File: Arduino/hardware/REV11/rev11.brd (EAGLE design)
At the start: 79 x 79 mm, 31 parts, among them IC2 ATMEGA168-AU, Q1 32768Hz

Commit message: updates to both rev10 and rev11
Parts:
- moved ANT 81.5 mm to (1.27, 34.9), turned to 0 degrees
- moved R1 79.0 mm to (74.9, 50.8)
- moved R3 79.0 mm to (74.9, 47.0)
- moved PHT1 73.3 mm to (76.2, 36.8)
- moved U$4 61.0 mm to (65.0, 2.73)
- moved JP1 52.3 mm to (30.5, 16.5), turned to 270 degrees
- moved U$1 49.8 mm to (76.9, 21.1)
- moved LED 45.4 mm to (47.4, 49.4), turned to 270 degrees
- moved R9 42.8 mm to (59.7, 21.6)
- moved U$2 41.7 mm to (82.4, 4.86)
- moved Q1 40.5 mm to (46.1, 27.9), turned to 270 degrees
- moved + 37.1 mm to (20.0, 43.5), turned to 0 degrees
- moved R7 36.6 mm to (47.7, 41.6), turned to 90 degrees
- moved RFM23B 33.3 mm to (58.8, 41.2), turned to 270 degrees
- moved C9 31.0 mm to (39.5, 27.4)
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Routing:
- net N$31: track 86.7 -> 85.1 mm
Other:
- board size 79 x 79 mm -> 72 x 53 mm
- board text added: "*"
- board text removed: "GND"

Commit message: updates to rev11
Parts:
- removed R3: (no value), resistor:0309V
- moved LED 26.5 mm to (69.7, 35.2), turned to 180 degrees
- moved PHT1 14.6 mm to (67.9, 48.9)
- moved R1 8.98 mm to (68.6, 44.5)
- moved ANT 2.00 mm to (1.27, 32.9)
- moved RFM23B 2.00 mm to (56.8, 41.2)
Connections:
- net GND: no longer R3.1
- net LDR: no longer R3.2

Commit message: updates to rev11
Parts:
- moved R7 21.5 mm to (67.0, 32.4), turned to 0 degrees
- moved R1 16.9 mm to (52.1, 48.3)
- moved PHT1 8.94 mm to (59.0, 48.9)
- moved Q1 4.58 mm to (42.3, 25.3)
- moved C7 4.02 mm to (51.4, 24.9)
- moved C4 4.02 mm to (54.9, 24.9)
- moved C8 4.02 mm to (59.0, 24.9)
- moved RFM23B 3.82 mm to (56.5, 37.4)
- moved C11 3.81 mm to (59.9, 15.1)
- moved R10 3.81 mm to (59.9, 10.9)
- moved R5 3.81 mm to (59.9, 3.91)
- moved R4 3.81 mm to (59.9, 7.72)
- moved R9 3.81 mm to (59.7, 17.8)
- moved C9 2.84 mm to (37.0, 28.6)
- moved LED 2.79 mm to (67.1, 36.0), turned to 270 degrees
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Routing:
- net N$31: track 85.1 -> 86.0 mm
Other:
- board size 72 x 53 mm -> 71 x 53 mm

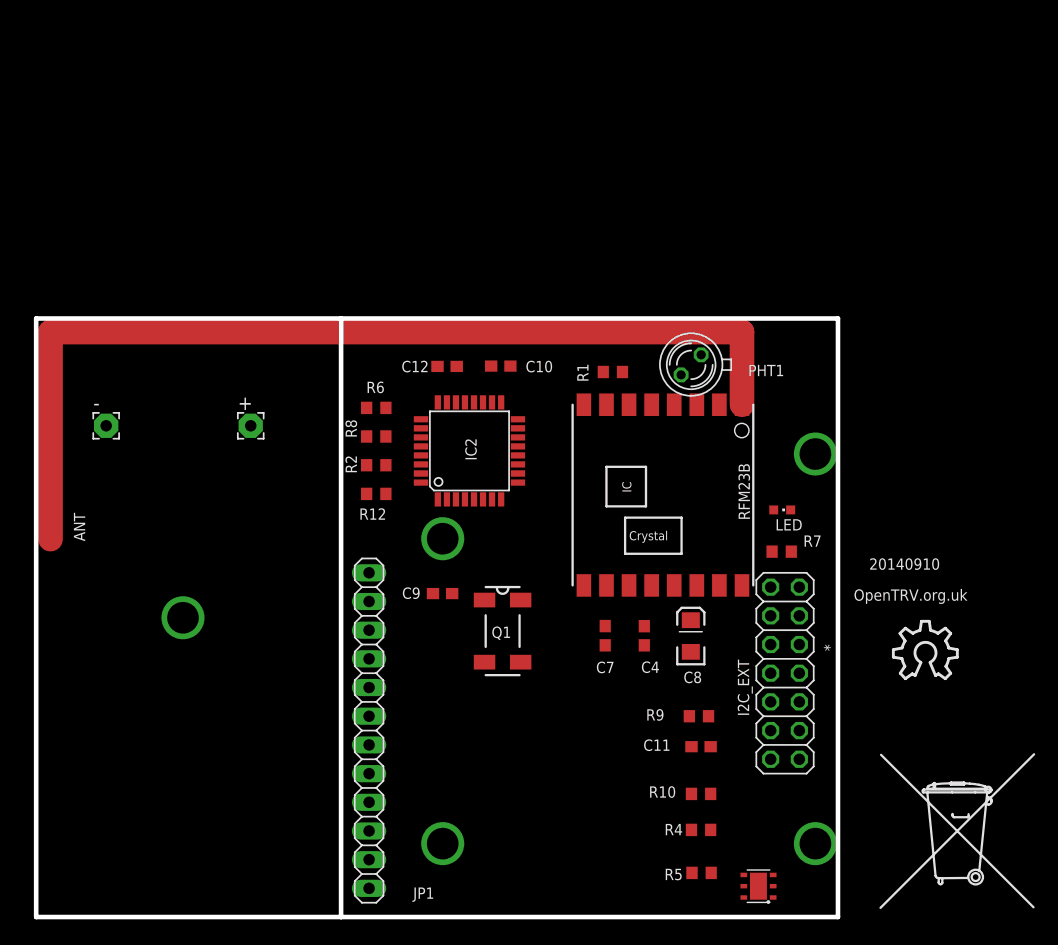
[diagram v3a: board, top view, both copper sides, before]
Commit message: updates to rev 10 & 11
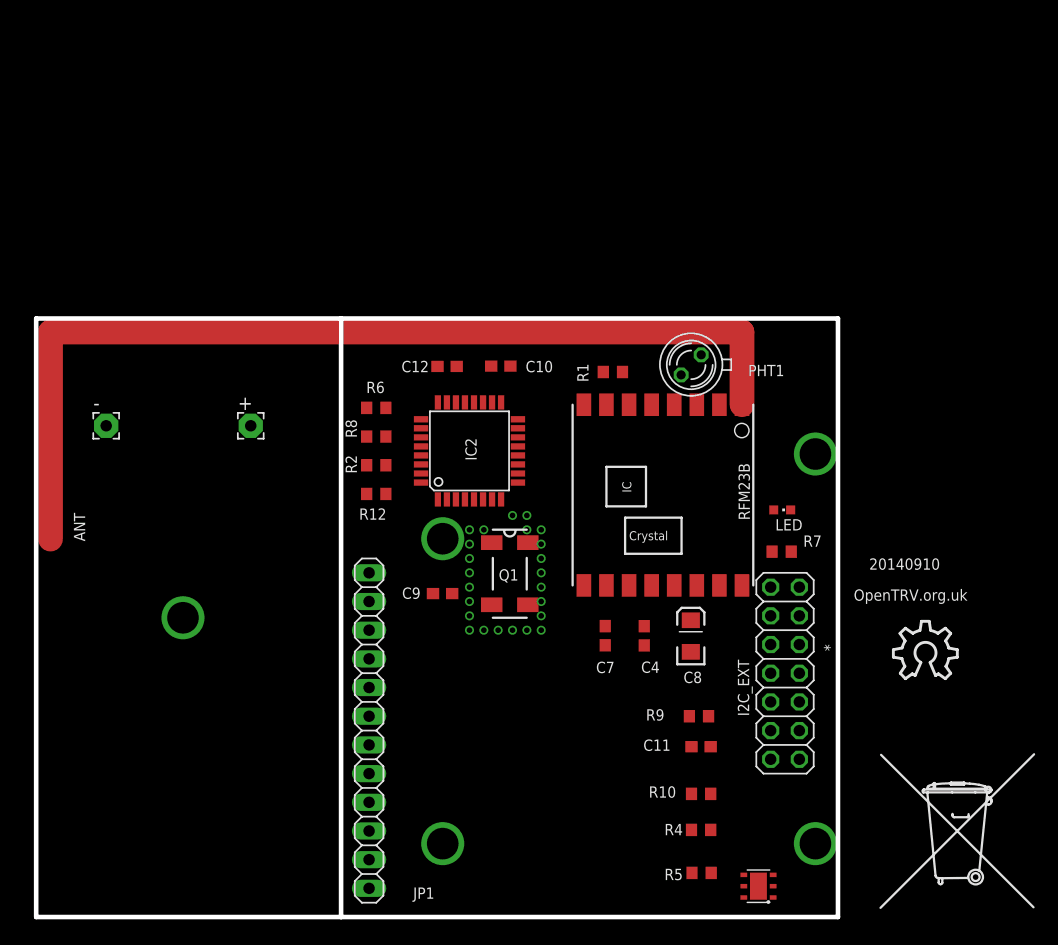
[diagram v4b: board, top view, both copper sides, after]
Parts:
- moved Q1 5.12 mm to (42.9, 30.4)
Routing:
- added copper zone on layer 16, net GND
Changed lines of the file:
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@@
 <attribute name="NAME" x="28.4" y="40.90808125" size="1" layer="25" font="vector" rot="R270"/>
 </element>
-<element name="Q1" library="crystal" package="MC-306" value="32768Hz" x="42.303484375" y="25.3201125" smashed="yes" rot="R270">
-<attribute name="OC_NEWARK" value="31M5576" x="42.303484375" y="25.3201125" size="1.778" layer="27" rot="R270" display="off"/>
-<attribute name="MPN" value="MC-306 60.0KHZ  100PPM ,12.5PF" x="42.303484375" y="25.3201125" size="1.778" layer="27" rot="R270" display="off"/>
-<attribute name="MF" value="" x="42.303484375" y="25.3201125" size="1.778" layer="27" rot="R270" display="off"/>
-<attribute name="OC_FARNELL" value="1278040" x="42.303484375" y="25.3201125" size="1.778" layer="27" rot="R270" display="off"/>
-<attribute name="NAME" x="43.0779125" y="25.711959375" size="1" layer="25" font="vector" rot="R180"/>
+<element name="Q1" library="crystal" package="MC-306" value="32768Hz" x="42.938484375" y="30.4001125" smashed="yes" rot="R270">
+<attribute name="OC_NEWARK" value="31M5576" x="42.938484375" y="30.4001125" size="1.778" layer="27" rot="R270" display="off"/>
+<attribute name="MPN" value="MC-306 60.0KHZ  100PPM ,12.5PF" x="42.938484375" y="30.4001125" size="1.778" layer="27" rot="R270" display="off"/>
+<attribute name="MF" value="" x="42.938484375" y="30.4001125" size="1.778" layer="27" rot="R270" display="off"/>
+<attribute name="OC_FARNELL" value="1278040" x="42.938484375" y="30.4001125" size="1.778" layer="27" rot="R270" display="off"/>
+<attribute name="NAME" x="43.7129125" y="30.791959375" size="1" layer="25" font="vector" rot="R180"/>
 </element>
 <element name="C9" library="resistor" package="C0603" value="100nF" x="36.988065625" y="28.641453125" smashed="yes">
@@
 <wire x1="30.48" y1="2.54" x2="37.838065625" y2="28.641453125" width="0" layer="19" extent="1-1"/>
 <wire x1="7.2" y1="43.5" x2="36.5393875" y2="48.75630625" width="0" layer="19" extent="1-1"/>
+<polygon width="0.4064" layer="16">
+<vertex x="1" y="53"/>
+<vertex x="1" y="0"/>
+<vertex x="72" y="0"/>
+<vertex x="72" y="53"/>
+</polygon>
 </signal>
 <signal name="D6">
@@
 <contactref element="Q1" pad="4"/>
 <contactref element="IC2" pad="8"/>
-<wire x1="42.17" y1="36.9824" x2="43.903484375" y2="28.0701125" width="0" layer="19" extent="1-1"/>
+<wire x1="42.17" y1="36.9824" x2="44.538484375" y2="33.1501125" width="0" layer="19" extent="1-1"/>
 </signal>
 <signal name="XTAL2">
 <contactref element="Q1" pad="1"/>
 <contactref element="IC2" pad="7"/>
-<wire x1="40.703484375" y1="28.0701125" x2="41.37" y2="36.9824" width="0" layer="19" extent="1-1"/>
+<wire x1="41.338484375" y1="33.1501125" x2="41.37" y2="36.9824" width="0" layer="19" extent="1-1"/>
 </signal>
 <signal name="TX">
@@
 <via x="70" y="6.5" extent="1-16" drill="2.8"/>
 </signal>
+<signal name="N$11">
+<via x="40.64" y="25.4" extent="1-16" drill="0.5"/>
+</signal>
+<signal name="N$12">
+<via x="41.91" y="25.4" extent="1-16" drill="0.5"/>
+</signal>
+<signal name="N$14">
+<via x="43.18" y="25.4" extent="1-16" drill="0.5"/>
+</signal>
+<signal name="N$15">
+<via x="44.45" y="25.4" extent="1-16" drill="0.5"/>
+</signal>
+<signal name="N$16">
+<via x="45.72" y="25.4" extent="1-16" drill="0.5"/>
+</signal>
+<signal name="N$17">
+<via x="45.72" y="26.67" extent="1-16" drill="0.5"/>
+</signal>
+<signal name="N$19">
+<via x="45.72" y="27.94" extent="1-16" drill="0.5"/>
+</signal>
+<signal name="N$20">
+<via x="45.72" y="29.21" extent="1-16" drill="0.5"/>
+</signal>
+<signal name="N$21">
+<via x="45.72" y="30.48" extent="1-16" drill="0.5"/>
+</signal>
+<signal name="N$22">
+<via x="45.72" y="31.75" extent="1-16" drill="0.5"/>
+</signal>
+<signal name="N$24">
+<via x="45.72" y="33.02" extent="1-16" drill="0.5"/>
+</signal>
+<signal name="N$25">
+<via x="45.72" y="34.29" extent="1-16" drill="0.5"/>
+</signal>
+<signal name="N$26">
+<via x="44.45" y="34.29" extent="1-16" drill="0.5"/>
+</signal>
+<signal name="N$28">
+<via x="44.45" y="35.56" extent="1-16" drill="0.5"/>
+</signal>
+<signal name="N$30">
+<via x="43.18" y="35.56" extent="1-16" drill="0.5"/>
+</signal>
+<signal name="N$32">
+<via x="39.37" y="33.02" extent="1-16" drill="0.5"/>
+</signal>
+<signal name="N$33">
+<via x="39.37" y="31.75" extent="1-16" drill="0.5"/>
+</signal>
+<signal name="N$34">
+<via x="39.37" y="30.48" extent="1-16" drill="0.5"/>
+</signal>
+<signal name="N$35">
+<via x="39.37" y="29.21" extent="1-16" drill="0.5"/>
+</signal>
+<signal name="N$36">
+<via x="39.37" y="27.94" extent="1-16" drill="0.5"/>
+</signal>
+<signal name="N$37">
+<via x="39.37" y="26.67" extent="1-16" drill="0.5"/>
+</signal>
+<signal name="N$38">
+<via x="39.37" y="25.4" extent="1-16" drill="0.5"/>
+</signal>
+<signal name="N$39">
+<via x="40.64" y="34.29" extent="1-16" drill="0.5"/>
+</signal>
+<signal name="N$40">
+<via x="39.37" y="34.29" extent="1-16" drill="0.5"/>
+</signal>
 </signals>

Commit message: bringing things back in sync
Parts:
- renumbered R1 to R1********
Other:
- board text added: "20151110"
- board text removed: "20140910"
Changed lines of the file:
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@@
 <board>
 <plain>
-<text x="81.041028125" y="31.75376875" size="1" layer="25" font="vector" rot="R180">20140910</text>
-<text x="73.245621875" y="1.250803125" size="1" layer="22" font="vector" rot="MR90">License: http://goo.gl/3d71UJ</text>
-<text x="73.391121875" y="28.01046875" size="1" layer="25" font="vector">OpenTRV.org.uk</text>
+<text x="48.021028125" y="16.51376875" size="1" layer="25" font="vector" rot="R180">20151110</text>
+<text x="26.689196875" y="0.855621875" size="1" layer="22" font="vector" rot="MR0">License: http://goo.gl/3d71UJ</text>
+<text x="41.641121875" y="2.61046875" size="1" layer="25" font="vector">OpenTRV.org.uk</text>
 <text x="70.353415625" y="24.155434375" size="1" layer="25" font="vector" rot="SR270">*</text>
 <wire x1="1" y1="53" x2="1" y2="0" width="0.4064" layer="20"/>
@@
 <attribute name="NAME" x="4.34" y="35.79" size="1" layer="25" rot="R270"/>
 </element>
-<element name="R1" library="resistor" package="R0603" value="220K" x="52.07" y="48.26" smashed="yes">
+<element name="R1********" library="resistor" package="R0603" value="220K" x="52.07" y="48.26" smashed="yes">
 <attribute name="NAME" x="49.911" y="47.371" size="1" layer="25" rot="R90"/>
 </element>
@@
 <contactref element="U$4" pad="2"/>
 <contactref element="I2C_EXT" pad="6"/>
-<contactref element="R1" pad="2"/>
+<contactref element="R1********" pad="2"/>
 <contactref element="JP1" pad="12"/>
 <contactref element="-" pad="1"/>
@@
 </signal>
 <signal name="LDR">
-<contactref element="R1" pad="1"/>
+<contactref element="R1********" pad="1"/>
 <contactref element="IC2" pad="23"/>
 <contactref element="PHT1" pad="K"/>

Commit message: Bo's update.
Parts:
- R1: value 220K -> 100K
- moved Q1 0.48 mm to (42.5, 30.2)
- renumbered R1******** to R1
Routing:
- net GND: track 0.00 -> 204.1 mm
- net VCC: track 0.00 -> 203.9 mm, vias 0 -> 7
- net SDA: track 0.00 -> 90.3 mm, vias 0 -> 4
- net D7: track 0.00 -> 89.6 mm, vias 0 -> 1
- net SCL: track 0.00 -> 80.7 mm, vias 0 -> 2
- net D2: track 0.00 -> 73.2 mm, vias 0 -> 3
- net SPI_NSS: track 0.00 -> 57.9 mm, vias 0 -> 4
- net TX: track 0.00 -> 52.8 mm, vias 0 -> 2
- net A7: track 0.00 -> 49.6 mm, vias 0 -> 1
- net RESET: track 0.00 -> 48.2 mm, vias 0 -> 4
- net RX: track 0.00 -> 47.9 mm, vias 0 -> 2
- net RFM_IRQ: track 0.00 -> 47.0 mm, vias 0 -> 2
- net SPI_MISO: track 0.00 -> 45.3 mm, vias 0 -> 2
- net SPI_MOSI: track 0.00 -> 44.7 mm, vias 0 -> 2
- net D6: track 0.00 -> 42.4 mm, vias 0 -> 3
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- added copper zone on layer 1, net GND
- removed copper zone on layer 16, net GND

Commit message: rev11 touch up
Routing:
- net A3: track 22.4 -> 62.0 mm, vias 1 -> 4
- net A7: track 49.6 -> 85.5 mm, vias 1 -> 3
- net SPI_NSS: track 57.9 -> 90.8 mm, vias 4 -> 6
- net LED_HEATCALL_L: track 33.0 -> 56.7 mm, vias 2 -> 4
- net SCL: track 80.7 -> 102.9 mm
- net GND: track 204.1 -> 224.6 mm
- net D7: track 89.6 -> 74.7 mm, vias 1 -> 3
- net SDA: track 90.3 -> 101.4 mm
- net RFM_IRQ: track 47.0 -> 57.4 mm
- net N$6: track 15.5 -> 5.27 mm, vias 4 -> 2
- net SPI_MISO: track 45.3 -> 35.4 mm, vias 2 -> 4
- net RX: track 47.9 -> 56.9 mm
- net N$4: track 19.7 -> 11.0 mm, vias 0 -> 1
- net A6: track 34.5 -> 42.0 mm, vias 1 -> 3
- net VCC: track 203.9 -> 210.4 mm, vias 7 -> 9
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- removed copper zone on layer 1, net GND

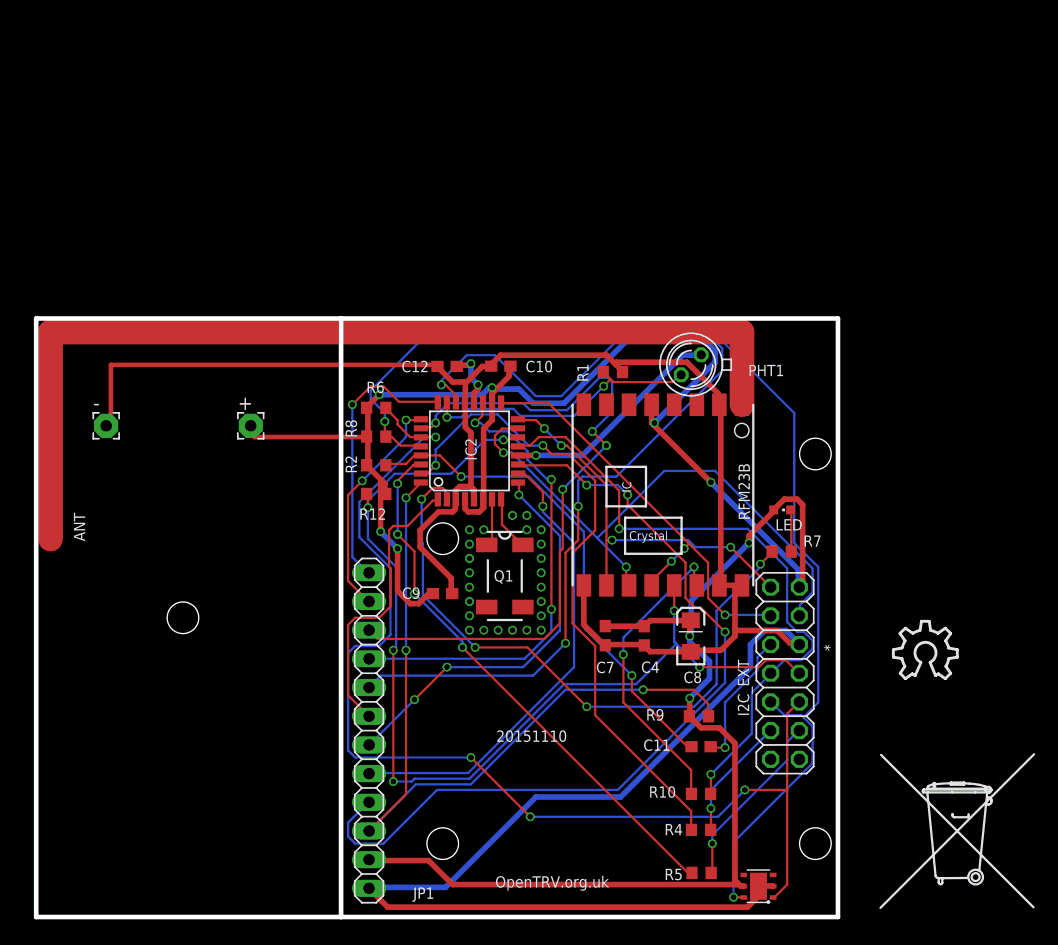
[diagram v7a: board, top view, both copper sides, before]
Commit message: rev10 and 11 updated as per deniz findings
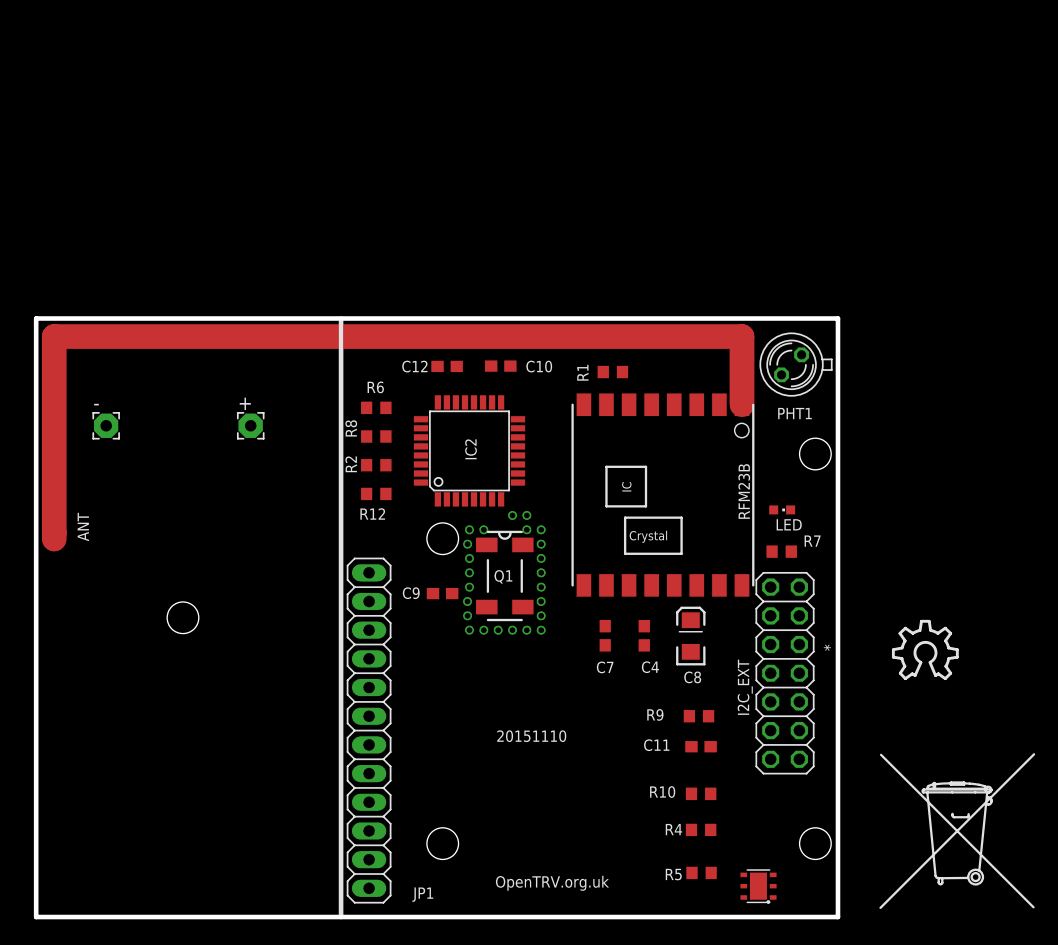
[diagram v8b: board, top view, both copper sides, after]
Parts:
- moved PHT1 8.89 mm to (67.9, 48.9)
- moved ANT 0.33 mm to (2.60, 34.0)
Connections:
- net D2: now also I2C_EXT.14
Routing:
- net GND: track 224.6 -> 0.00 mm
- net VCC: track 210.4 -> 0.00 mm, vias 9 -> 0
- net SCL: track 102.9 -> 0.00 mm, vias 2 -> 0
- net SDA: track 101.4 -> 0.00 mm, vias 4 -> 0
- net SPI_NSS: track 90.8 -> 0.00 mm, vias 6 -> 0
- net A7: track 85.5 -> 0.00 mm, vias 3 -> 0
- net D7: track 74.7 -> 0.00 mm, vias 3 -> 0
- net D2: track 69.6 -> 0.00 mm, vias 3 -> 0
- net A3: track 62.0 -> 0.00 mm, vias 4 -> 0
- net RFM_IRQ: track 57.4 -> 0.00 mm, vias 2 -> 0
- net RX: track 56.9 -> 0.00 mm, vias 2 -> 0
- net LED_HEATCALL_L: track 56.7 -> 0.00 mm, vias 4 -> 0
- net SPI_MOSI: track 50.7 -> 0.00 mm, vias 2 -> 0
- net TX: track 48.4 -> 0.00 mm, vias 4 -> 0
- net RESET: track 43.9 -> 0.00 mm, vias 2 -> 0
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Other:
- outline, holes or cut-outs redrawn
